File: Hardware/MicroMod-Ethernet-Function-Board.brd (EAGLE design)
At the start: 38 x 65 mm, 84 parts, among them J1 MAGJACK_SYM, J11 MICROMOD_STANDARD, Q5 20V/4.2A/52mΩ/1.4W, Q6 600mA/40V, U1 EEPROM, U2 AG980X, U3 W5500-ETHERNET, U4 3.3V, Y1 24MHz

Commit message: Update PoE module to DP990X.
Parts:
- removed U2: AG980X, Ethernet:AG980X
- added C25, C26: 10uF, SparkFun-Capacitors:0805
- added C8: 100uF, SparkFun-Capacitors:PANASONIC_D
- added ISO1, ISO2: (no value), SparkFun-Jumpers:COMBO-JUMPER_2_NC_TRACE
- added JP5: JUMPER-SMT_2_NO_SILK, SparkFun-Jumpers:SMT-JUMPER_2_NO_SILK
- added L1: 2.2uH, SparkFun-Coils:0805-WIDE
- added LOAD: (no value), SparkFun-Jumpers:SMT-JUMPER_2_NC_TRACE_SILK
- added R22: 10k, SparkFun-Resistors:0603
- added U$5: (no value), output:#DUMMY_LOAD#0
- added U$6: (no value), output:#WP#0
- added U5: POE_PSU-DP990X, Ethernet:DP990X
- C13: value 0.22uF -> 1.0uF
- C19: value 22uF -> 1nF
- C21, C22: value 10nF -> 6.8nF
- C7: value 560uF/25V -> 10uF; device SparkFun-Capacitors:PANASONIC_G -> SparkFun-Capacitors:0805
- JP4: device SparkFun-Jumpers:SMT-JUMPER_2_NO_SILK -> SparkFun-Jumpers:SMT-JUMPER_2_NC_TRACE_SILK
- Q1: value 600mA/40V -> 220mA/50V/3.5Ω
- R13, R18, R19, R20: value 47 -> 49.9
- R2: value 470 -> 510; device SparkFun-Resistors:0603 -> SparkFun-Resistors:2010
- R6, R7: value 100k -> 10k
- R8: value 12.1k -> 12.4k
- U3: value W5500-ETHERNET -> W5500; device Ethernet:LQFP-48 -> SparkFun-IC-Comms:LQFP-48
- Y1: value 24MHz -> 25MHz
- moved R2 10.8 mm to (17.0, 15.0), turned to 0 degrees
- moved C7 8.54 mm to (21.0, 19.0), turned to 270 degrees
- moved LOGO1 4.12 mm to (4.19, 59.0)
- moved U$63 2.24 mm to (6.05, 60.0)
- moved C4 2.00 mm to (17.0, 11.0)
- renumbered PWR_LED to POE_LED, Q6 to Q1
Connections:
- removed net N$4: J11.71, R2.2
- new net 5V_FILTER: C26.1, D1.A, L1.2, LOAD.2, POE_LED.2
- new net N$12: JP5.2, R22.2, U1.7
- new net N$14: ISO1.2, ISO1.4, U5.5, U5.6
- new net N$18: ISO2.2, ISO2.4, U5.7, U5.8
- new net N$9: LOAD.1, R2.2
- net 3.3V: now also R22.1
- net 5V: no longer POE_LED.2
- net 5V_RAW: now also C25.1, C7.1, C8.+, L1.1, U5.1, U5.2; no longer C7.+, D1.A, U2.1, U2.2
- net GND: now also C25.2, C26.2, C7.2, C8.-, JP5.1, Q1.2, R2.1, U5.3; no longer C7.-, R7.1, U1.7, U2.3
- net N$11: now also R7.1; no longer R7.2
- net PW+: now also ISO1.1, ISO1.3; no longer U2.5, U2.6
- net PW-: now also ISO2.1, ISO2.3; no longer U2.7, U2.8
- net PWR_EN: now also J11.71; no longer R2.1
- net VCC_IN: now also R7.2; no longer Q1.2
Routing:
- net N$18: track 0.00 -> 40.5 mm, vias 0 -> 1
- net PW-: track 46.2 -> 5.92 mm, vias 1 -> 0
- net 5V_FILTER: track 0.00 -> 31.1 mm, vias 0 -> 3
- net PW+: track 28.6 -> 7.09 mm, vias 1 -> 0
- net N$14: track 0.00 -> 21.1 mm, vias 0 -> 1
- net N$12: track 0.00 -> 9.10 mm, vias 0 -> 3
- net PWR_EN: track 46.1 -> 51.5 mm
- net N$9: track 0.00 -> 5.27 mm, vias 0 -> 1
- net N$4: track 3.96 -> 0.00 mm
- net 3.3V: track 92.6 -> 96.4 mm
- net 5V: track 12.4 -> 9.37 mm
- net VCC_IN: track 30.7 -> 33.0 mm
- net 3.3V_IN: track 13.4 -> 15.1 mm, vias 2 -> 0
- net 5V_RAW: track 17.4 -> 16.2 mm
- net GND-ISO: track 26.7 -> 25.6 mm
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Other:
- outline, holes or cut-outs redrawn

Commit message: Add x01 panel files
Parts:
- added LED1, LED2: JUMPER-SMT_2_NC_TRACE_SILK, SparkFun-Jumpers:SMT-JUMPER_2_NC_TRACE_SILK
- added R23, R24, R30, R4: 10k, SparkFun-Resistors:0603
- added U$12: (no value), output:#LNK#1
- added U$19: (no value), output:#POE#0
- added U$8: (no value), output:#ACT#0
- R3, R5: value 330 -> 1k
- moved C7 2.01 mm to (21.2, 17.0)
- moved C16 2.00 mm to (25.0, 24.0)
- moved C25 2.00 mm to (23.0, 17.0)
- moved D1 2.00 mm to (25.0, 20.0)
- moved FB2 2.00 mm to (25.0, 22.0)
- moved L1 2.00 mm to (25.0, 17.0)
- flipped ISO1 to the bottom, turned to 0 degrees
- flipped ISO2 to the bottom, turned to 0 degrees
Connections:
- new net N$17: R30.2, U3.23
- new net N$3: J1.14, LED2.1
- new net N$4: J1.12, LED1.1
- net 3.3V: now also R23.2, R24.2, R4.2
- net ACT_LED: now also LED2.2; no longer J1.14
- net ETH_!CS!: now also R23.1
- net ETH_!INT!: now also R4.1
- net ETH_!RST!: now also R24.1
- net GND: now also R30.1
- net LINK_LED: now also LED1.2; no longer J1.12
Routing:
- net N$3: track 0.00 -> 24.2 mm
- net ACT_LED: track 55.9 -> 33.1 mm
- net 3.3V: track 96.4 -> 107.9 mm, vias 7 -> 8
- net N$4: track 0.00 -> 8.36 mm
- net LINK_LED: track 42.0 -> 34.4 mm
- net ETH_!INT!: track 40.0 -> 47.4 mm, vias 2 -> 4
- net ETH_!RST!: track 46.4 -> 53.3 mm
- net N$17: track 0.00 -> 5.76 mm
- net ETH_!CS!: track 37.0 -> 41.3 mm, vias 2 -> 3
- net VCCA: track 53.2 -> 55.2 mm
- net 5V_FILTER: track 31.1 -> 33.1 mm
- net N$7: track 5.35 -> 6.97 mm
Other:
- outline, holes or cut-outs redrawn

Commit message: Update PROD_IDs
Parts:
- J1: value MAGJACK_SYM -> MAGJACK-POE; device Ethernet:MAGJACK-STR_LED -> SparkFun-Connectors:MAGJACK-SYM_LED
- R2: value 510 -> 49.9 1/2W; device SparkFun-Resistors:2010 -> SparkFun-Resistors:1206
- U5: device Ethernet:DP990X -> SparkFun-IC-Power:DP990X

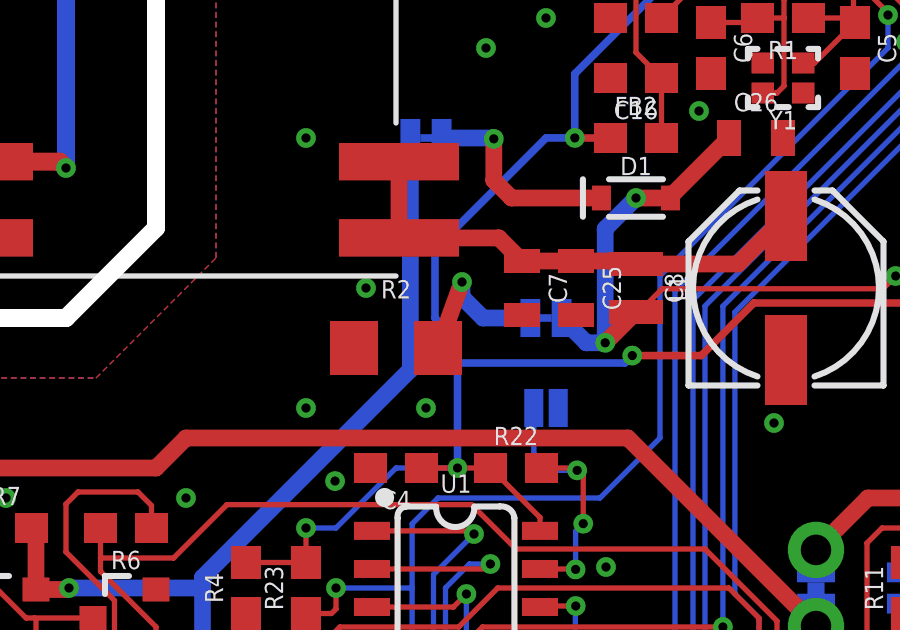
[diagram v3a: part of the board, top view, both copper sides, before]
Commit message: Change load resistor to 1206.
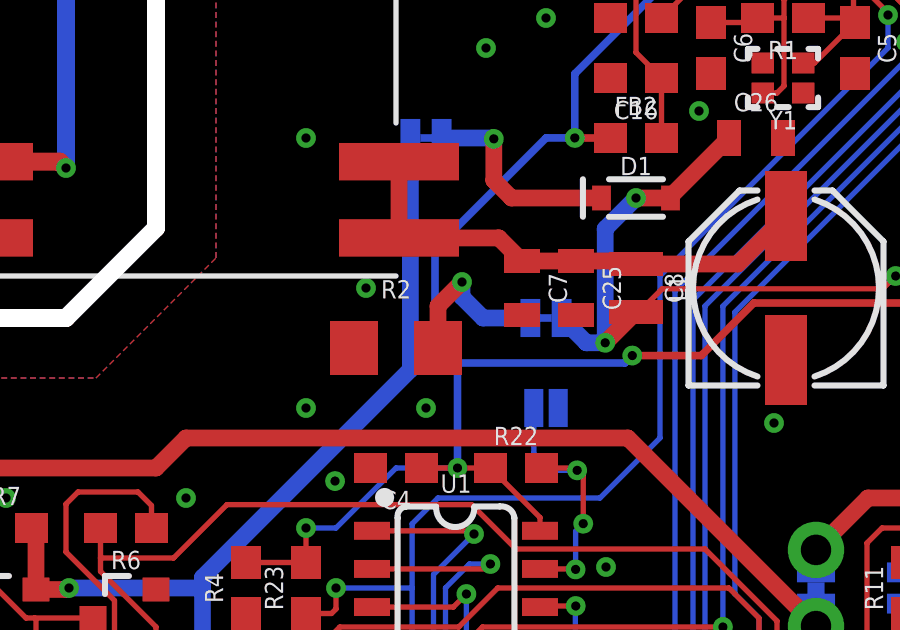
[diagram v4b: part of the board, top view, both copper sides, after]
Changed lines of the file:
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@@
 <setting verticaltext="up"/>
 </settings>
-<grid distance="0.05" unitdist="inch" unit="inch" style="lines" multiple="1" display="yes" altdistance="0.005" altunitdist="inch" altunit="inch"/>
+<grid distance="1" unitdist="mm" unit="mm" style="lines" multiple="1" display="yes" altdistance="0.1" altunitdist="mm" altunit="mm"/>
 <layers>
 <layer number="1" name="Top/Horz" color="4" fill="1" visible="yes" active="yes"/>
@@
 <contactref element="R30" pad="1"/>
 <via x="12" y="4" extent="1-16" drill="0.3048"/>
-<wire x1="35.75" y1="44" x2="37.05" y2="46.1" width="0" layer="19" extent="1-1"/>
-<wire x1="31" y1="41" x2="35.75" y2="44" width="0" layer="19" extent="1-1"/>
-<wire x1="31" y1="39.85" x2="31" y2="41" width="0" layer="19" extent="1-1"/>
-<wire x1="29" y1="39.85" x2="31" y2="39.85" width="0" layer="19" extent="1-1"/>
-<wire x1="27" y1="39.85" x2="29" y2="39.85" width="0" layer="19" extent="1-1"/>
-<wire x1="27" y1="41" x2="27" y2="39.85" width="0" layer="19" extent="1-1"/>
-<wire x1="25" y1="41" x2="27" y2="41" width="0" layer="19" extent="1-1"/>
-<wire x1="25" y1="39.85" x2="25" y2="41" width="0" layer="19" extent="1-1"/>
-<wire x1="23" y1="40" x2="25" y2="39.85" width="0" layer="19" extent="1-1"/>
-<wire x1="24" y1="44" x2="25" y2="41" width="0" layer="19" extent="1-1"/>
-<wire x1="24" y1="45.15" x2="24" y2="44" width="0" layer="19" extent="1-1"/>
-<wire x1="22" y1="45.15" x2="24" y2="45.15" width="0" layer="19" extent="1-1"/>
-<wire x1="22" y1="44" x2="22" y2="45.15" width="0" layer="19" extent="1-1"/>
-<wire x1="30.75" y1="36.25" x2="31" y2="39.85" width="0" layer="19" extent="1-1"/>
-<wire x1="29.446" y1="34.527" x2="30.75" y2="36.25" width="0" layer="19" extent="1-1"/>
-<wire x1="29.4" y1="33.2" x2="29.446" y2="34.527" width="0" layer="19" extent="1-1"/>
-<wire x1="29.4" y1="31.7" x2="29.4" y2="33.2" width="0" layer="19" extent="1-1"/>
-<wire x1="27.75" y1="33.25" x2="29.4" y2="33.2" width="0" layer="19" extent="1-1"/>
-<wire x1="27.75" y1="34.25" x2="27.75" y2="33.25" width="0" layer="19" extent="1-1"/>
-<wire x1="27.75" y1="31.75" x2="27.75" y2="33.25" width="0" layer="19" extent="1-1"/>
-<wire x1="27.2" y1="36" x2="27.75" y2="34.25" width="0" layer="19" extent="1-1"/>
-<wire x1="33.75" y1="36.25" x2="30.75" y2="36.25" width="0" layer="19" extent="1-1"/>
-<wire x1="33.5936" y1="34" x2="33.75" y2="36.25" width="0" layer="19" extent="1-16"/>
-<wire x1="32.7" y1="33.9" x2="33.5936" y2="34" width="0" layer="19" extent="16-16"/>
-<wire x1="33.5936" y1="32" x2="33.5936" y2="34" width="0" layer="19" extent="16-16"/>
-<wire x1="33.5936" y1="30" x2="33.5936" y2="32" width="0" layer="19" extent="16-16"/>
-<wire x1="32" y1="29.6" x2="33.5936" y2="30" width="0" layer="19" extent="16-16"/>
-<wire x1="31.25" y1="27.75" x2="32" y2="29.6" width="0" layer="19" extent="1-1"/>
-<wire x1="36.25" y1="34.75" x2="33.5936" y2="34" width="0" layer="19" extent="1-16"/>
-<wire x1="36.5" y1="35.6" x2="36.25" y2="34.75" width="0" layer="19" extent="1-1"/>
-<wire x1="24.15" y1="36" x2="27.2" y2="36" width="0" layer="19" extent="1-1"/>
-<wire x1="23" y1="36.2" x2="24.15" y2="36" width="0" layer="19" extent="1-1"/>
-<wire x1="24.15" y1="34" x2="24.15" y2="36" width="0" layer="19" extent="1-1"/>
-<wire x1="24.15" y1="32" x2="24.15" y2="34" width="0" layer="19" extent="1-1"/>
-<wire x1="23" y1="32" x2="24.15" y2="32" width="0" layer="19" extent="1-1"/>
-<wire x1="24.15" y1="30" x2="24.15" y2="32" width="0" layer="19" extent="1-1"/>
-<wire x1="23" y1="30" x2="24.15" y2="30" width="0" layer="19" extent="1-1"/>
-<wire x1="24.15" y1="28" x2="24.15" y2="30" width="0" layer="19" extent="1-1"/>
-<wire x1="21" y1="32" x2="23" y2="32" width="0" layer="19" extent="1-1"/>
-<wire x1="24.15" y1="26" x2="24.15" y2="28" width="0" layer="19" extent="1-1"/>
-<wire x1="24.15" y1="24" x2="24.15" y2="26" width="0" layer="19" extent="1-1"/>
-<wire x1="22" y1="28" x2="24.15" y2="28" width="0" layer="19" extent="1-1"/>
-<wire x1="22" y1="26" x2="22" y2="28" width="0" layer="19" extent="1-1"/>
-<wire x1="20" y1="25" x2="22" y2="26" width="0" layer="19" extent="1-1"/>
-<wire x1="20.2" y1="35.2" x2="23" y2="36.2" width="0" layer="19" extent="1-1"/>
-<wire x1="27.1" y1="22.9" x2="24.15" y2="24" width="0" layer="19" extent="1-1"/>
-<wire x1="27.5" y1="24.15" x2="27.1" y2="22.9" width="0" layer="19" extent="1-1"/>
-<wire x1="28" y1="27" x2="27.5" y2="24.15" width="0" layer="19" extent="1-1"/>
-<wire x1="29.9" y1="22" x2="27.1" y2="22.9" width="0" layer="19" extent="1-1"/>
-<wire x1="17.1" y1="34.79" x2="20.2" y2="35.2" width="0" layer="19" extent="1-1"/>
-<wire x1="14.1" y1="35.2" x2="17.1" y2="34.79" width="0" layer="19" extent="1-1"/>
-<wire x1="32.3" y1="24.15" x2="29.9" y2="22" width="0" layer="19" extent="1-1"/>
-<wire x1="36" y1="23" x2="32.3" y2="24.15" width="0" layer="19" extent="1-1"/>
-<wire x1="36.84" y1="22.05" x2="36" y2="23" width="0" layer="19" extent="1-1"/>
-<wire x1="36.85" y1="20" x2="36.84" y2="22.05" width="0" layer="19" extent="1-1"/>
-<wire x1="36.85" y1="18" x2="36.85" y2="20" width="0" layer="19" extent="1-1"/>
-<wire x1="36" y1="15" x2="36.85" y2="18" width="0" layer="19" extent="1-1"/>
-<wire x1="36" y1="13.6999" x2="36" y2="15" width="0" layer="19" extent="1-1"/>
-<wire x1="36.85" y1="12" x2="36" y2="13.6999" width="0" layer="19" extent="1-1"/>
-<wire x1="36.85" y1="10" x2="36.85" y2="12" width="0" layer="19" extent="1-1"/>
-<wire x1="37" y1="8.6" x2="36.85" y2="10" width="0" layer="19" extent="1-1"/>
-<wire x1="36" y1="6.877" x2="37" y2="8.6" width="0" layer="19" extent="1-1"/>
-<wire x1="30" y1="14.6" x2="36" y2="15" width="0" layer="19" extent="1-1"/>
-<wire x1="29.6" y1="12.5" x2="30" y2="14.6" width="0" layer="19" extent="1-1"/>
-<wire x1="14" y1="22" x2="20" y2="25" width="0" layer="19" extent="1-1"/>
-<wire x1="16" y1="17" x2="14" y2="22" width="0" layer="19" extent="1-1"/>
-<wire x1="15.6" y1="15" x2="16" y2="17" width="0" layer="19" extent="1-1"/>
-<wire x1="14" y1="13" x2="15.6" y2="15" width="0" layer="19" extent="1-1"/>
-<wire x1="14.968" y1="10.565" x2="14" y2="13" width="0" layer="19" extent="1-1"/>
-<wire x1="16.15" y1="11" x2="14.968" y2="10.565" width="0" layer="19" extent="1-1"/>
-<wire x1="18" y1="13" x2="16.15" y2="11" width="0" layer="19" extent="1-1"/>
-<wire x1="22.4064" y1="13" x2="18" y2="13" width="0" layer="19" extent="16-16"/>
-<wire x1="23" y1="16.1" x2="22.4064" y2="13" width="0" layer="19" extent="1-16"/>
-<wire x1="21.2" y1="16.1" x2="23" y2="16.1" width="0" layer="19" extent="1-1"/>
-<wire x1="10" y1="10" x2="14" y2="13" width="0" layer="19" extent="1-1"/>
-<wire x1="9" y1="6.95" x2="10" y2="10" width="0" layer="19" extent="1-1"/>
-<wire x1="9.7" y1="3.4" x2="9" y2="6.95" width="0" layer="19" extent="1-1"/>
-<wire x1="9.8" y1="1.275" x2="9.7" y2="3.4" width="0" layer="19" extent="1-1"/>
-<wire x1="12" y1="4" x2="9.7" y2="3.4" width="0" layer="19" extent="1-1"/>
-<wire x1="15.6" y1="4" x2="12" y2="4" width="0" layer="19" extent="1-1"/>
-<wire x1="16.2" y1="5.095" x2="15.6" y2="4" width="0" layer="19" extent="1-1"/>
-<wire x1="18.3" y1="3.1" x2="15.6" y2="4" width="0" layer="19" extent="1-1"/>
-<wire x1="18.8" y1="1.275" x2="18.3" y2="3.1" width="0" layer="19" extent="1-1"/>
-<wire x1="20.3" y1="1.275" x2="18.8" y2="1.275" width="0" layer="19" extent="1-1"/>
-<wire x1="17.3" y1="1.275" x2="18.8" y2="1.275" width="0" layer="19" extent="1-1"/>
-<wire x1="20.7" y1="3.8" x2="18.3" y2="3.1" width="0" layer="19" extent="1-1"/>
-<wire x1="24" y1="7.7" x2="20.7" y2="3.8" width="0" layer="19" extent="1-1"/>
-<wire x1="28.3" y1="4.7" x2="24" y2="7.7" width="0" layer="19" extent="1-1"/>
-<wire x1="4" y1="10" x2="9" y2="6.95" width="0" layer="19" extent="1-1"/>
-<wire x1="12" y1="42" x2="14.1" y2="35.2" width="0" layer="19" extent="1-1"/>
-<wire x1="10.4" y1="42" x2="12" y2="42" width="0" layer="19" extent="1-1"/>
-<wire x1="2.35" y1="44" x2="10.4" y2="42" width="0" layer="19" extent="1-1"/>
+<wire x1="10.4" y1="42" x2="2.35" y2="44" width="0" layer="19" extent="1-1"/>
 </signal>
 <signal name="3.3V">
@@
 <contactref element="LOAD" pad="1"/>
 <contactref element="R2" pad="2"/>
-<wire x1="18.4" y1="15" x2="19.2" y2="17.2" width="0.5588" layer="1"/>
 <via x="19.2" y="17.2" extent="1-16" drill="0.3048"/>
 <wire x1="19.2" y1="17.2" x2="19.2" y2="16.7" width="0.5588" layer="16"/>
 <wire x1="19.2" y1="16.7" x2="19.9" y2="16" width="0.5588" layer="16"/>
 <wire x1="19.9" y1="16" x2="21.4793" y2="16" width="0.5588" layer="16"/>
+<wire x1="18.4" y1="15" x2="18.4" y2="16.4" width="0.5588" layer="1"/>
+<wire x1="18.4" y1="16.4" x2="19.2" y2="17.2" width="0.5588" layer="1"/>
 </signal>
 <signal name="N$14">

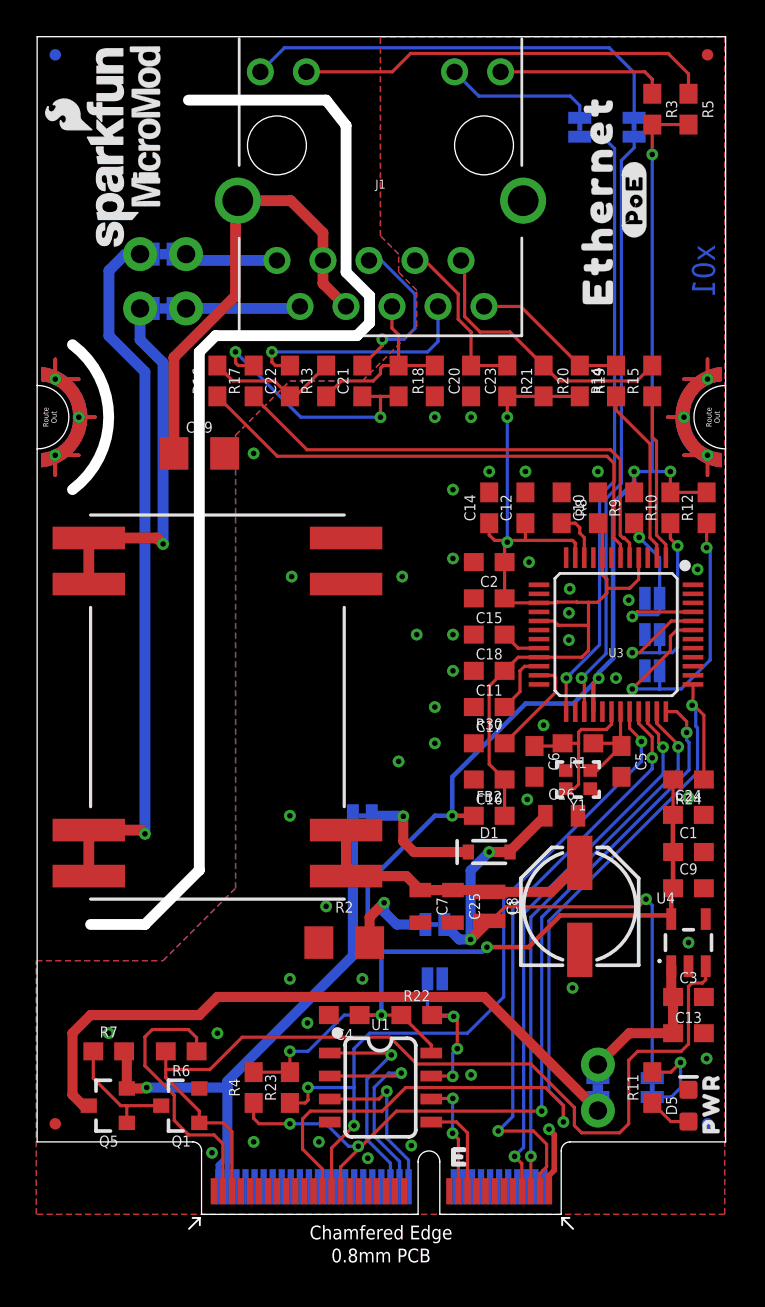
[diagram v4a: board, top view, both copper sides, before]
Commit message: Connect PWR LED to 3.3V rail. Add POE LED. Add pin 1 indicator to PoE module. Add hot caution.
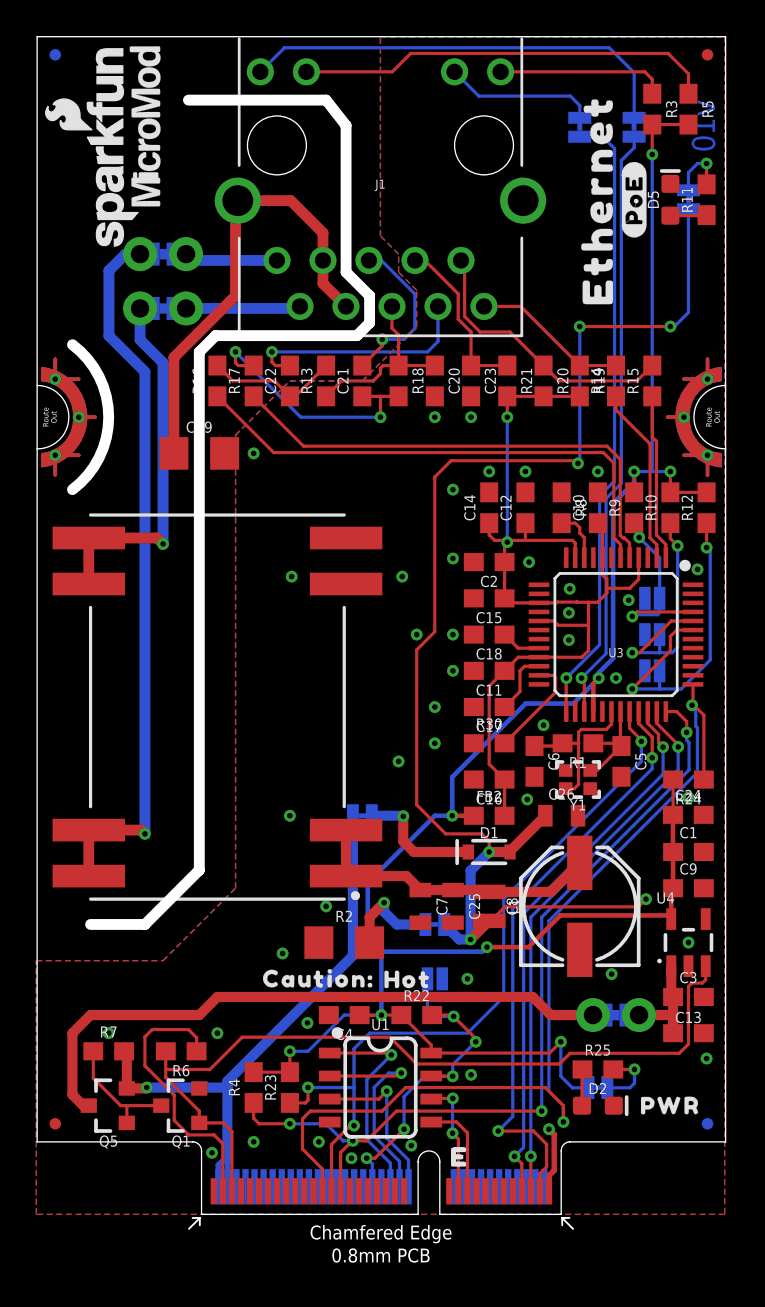
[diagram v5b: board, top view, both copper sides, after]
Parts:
- removed U$9: (no value), output:#PWR#0
- added D2: RED, SparkFun-LED:LED-0603
- added PWR_LED: JUMPER-SMT_2_NC_TRACE_SILK, SparkFun-Jumpers:SMT-JUMPER_2_NC_TRACE_SILK
- added R25: 1k, SparkFun-Resistors:0603
- added U$20: (no value), output:CAUTION#0
- added U$21: (no value), output:HOT#1
- added U$22: (no value), output:#PWR#0
- D5: value RED -> Yellow
- ISO1, ISO2, MEAS: value (none) -> JUMPER-COMBO_2_NC_TRACE
- JP1, JP2, JP3: value (none) -> JUMPER-SMT_2_NO_SILK
- LOAD, POE_LED: value (none) -> JUMPER-SMT_2_NC_TRACE_SILK
- moved D5 50.0 mm to (35.0, 56.0)
- moved R11 49.1 mm to (37.0, 56.0)
- moved POE_LED 49.0 mm to (36.0, 56.0), turned to 270 degrees
- moved MEAS 4.12 mm to (32.0, 11.0), turned to 180 degrees
- moved U$28 3.40 mm to (30.2, 11.0), turned to 0 degrees
- moved U$7 2.25 mm to (35.0, 6.00), turned to 0 degrees
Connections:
- removed net N$12: JP5.2, R22.2, U1.7
- new net EWP: J11.40, JP5.2, R22.2, U1.7
- new net N$19: PWR_LED.1, R25.2
- new net N$20: D2.A, R25.1
- net 3.3V: now also PWR_LED.2
- net GND: now also D2.C
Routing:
- net 5V_FILTER: track 33.1 -> 75.0 mm, vias 3 -> 6
- net EWP: track 0.00 -> 19.3 mm, vias 0 -> 5
- net 3.3V: track 107.9 -> 119.0 mm, vias 8 -> 9
- net N$12: track 9.10 -> 0.00 mm, vias 3 -> 0
- net PWR_EN: track 51.5 -> 45.7 mm
- net N$19: track 0.00 -> 3.54 mm, vias 0 -> 1
- net 5V: track 9.37 -> 6.38 mm
- net VCC: track 37.7 -> 35.3 mm
- net N$20: track 0.00 -> 2.01 mm
- net N$6: track 4.95 -> 3.34 mm
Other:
- board text added: "v10"
- board text removed: "x01"
